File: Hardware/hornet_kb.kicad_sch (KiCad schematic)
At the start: 0 parts

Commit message: Put in mcu and pwoer sheet
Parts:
- added J1: Conn_ST_STDC14, symbol Connector:Conn_ST_STDC14
- added U1: nRF52840, Package_DFN_QFN:Nordic_AQFN-73-1EP_7x7mm_P0.5mm, symbol MCU_Nordic:nRF52840
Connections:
- new net: U1.A22 (VDD), U1.AD14 (VDD), U1.AD23 (VDD), U1.B1 (VDD), U1.W1 (VDD)
- new net: U1.B7 (VSS), U1.EP (VSS)
- new net: J1.5 (GND), J1.7 (GND)
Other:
- added sheet Power Management (power_management.kicad_sch)
- title: (none) -> Hornet Wireless Split Keyboard

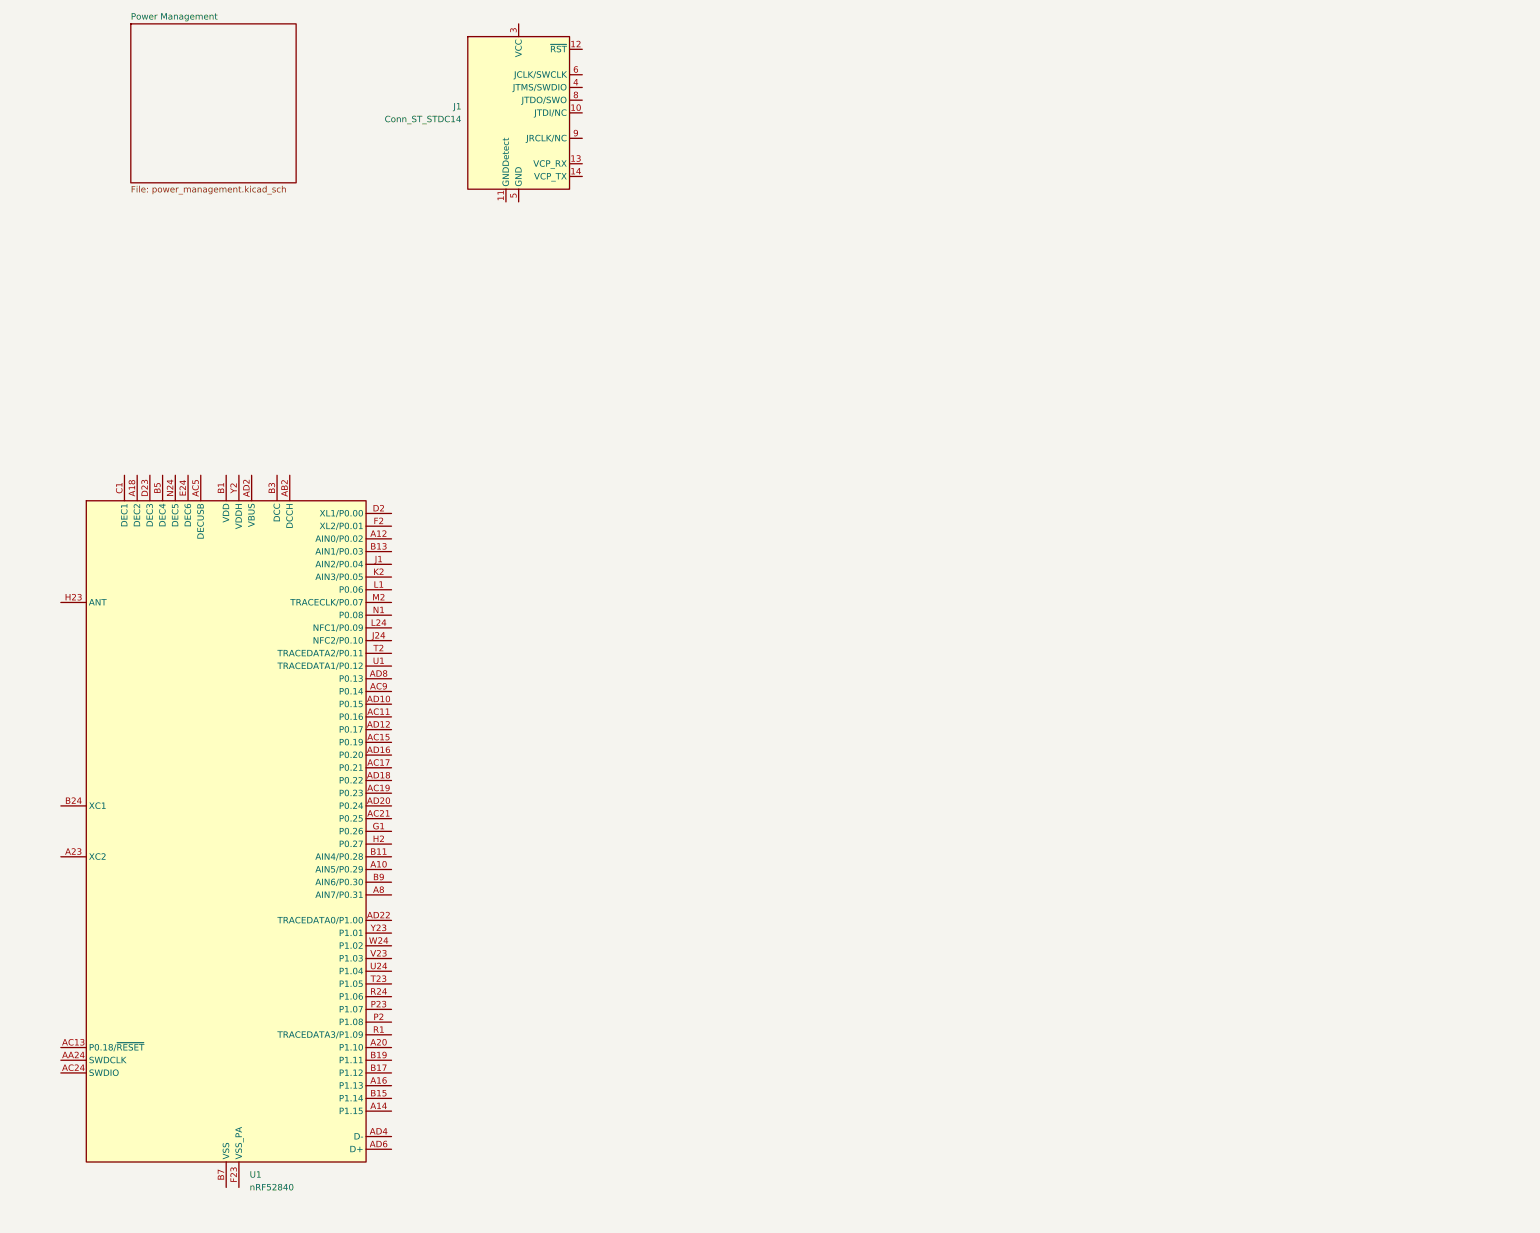
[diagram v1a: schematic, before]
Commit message: Added programmer and usbc
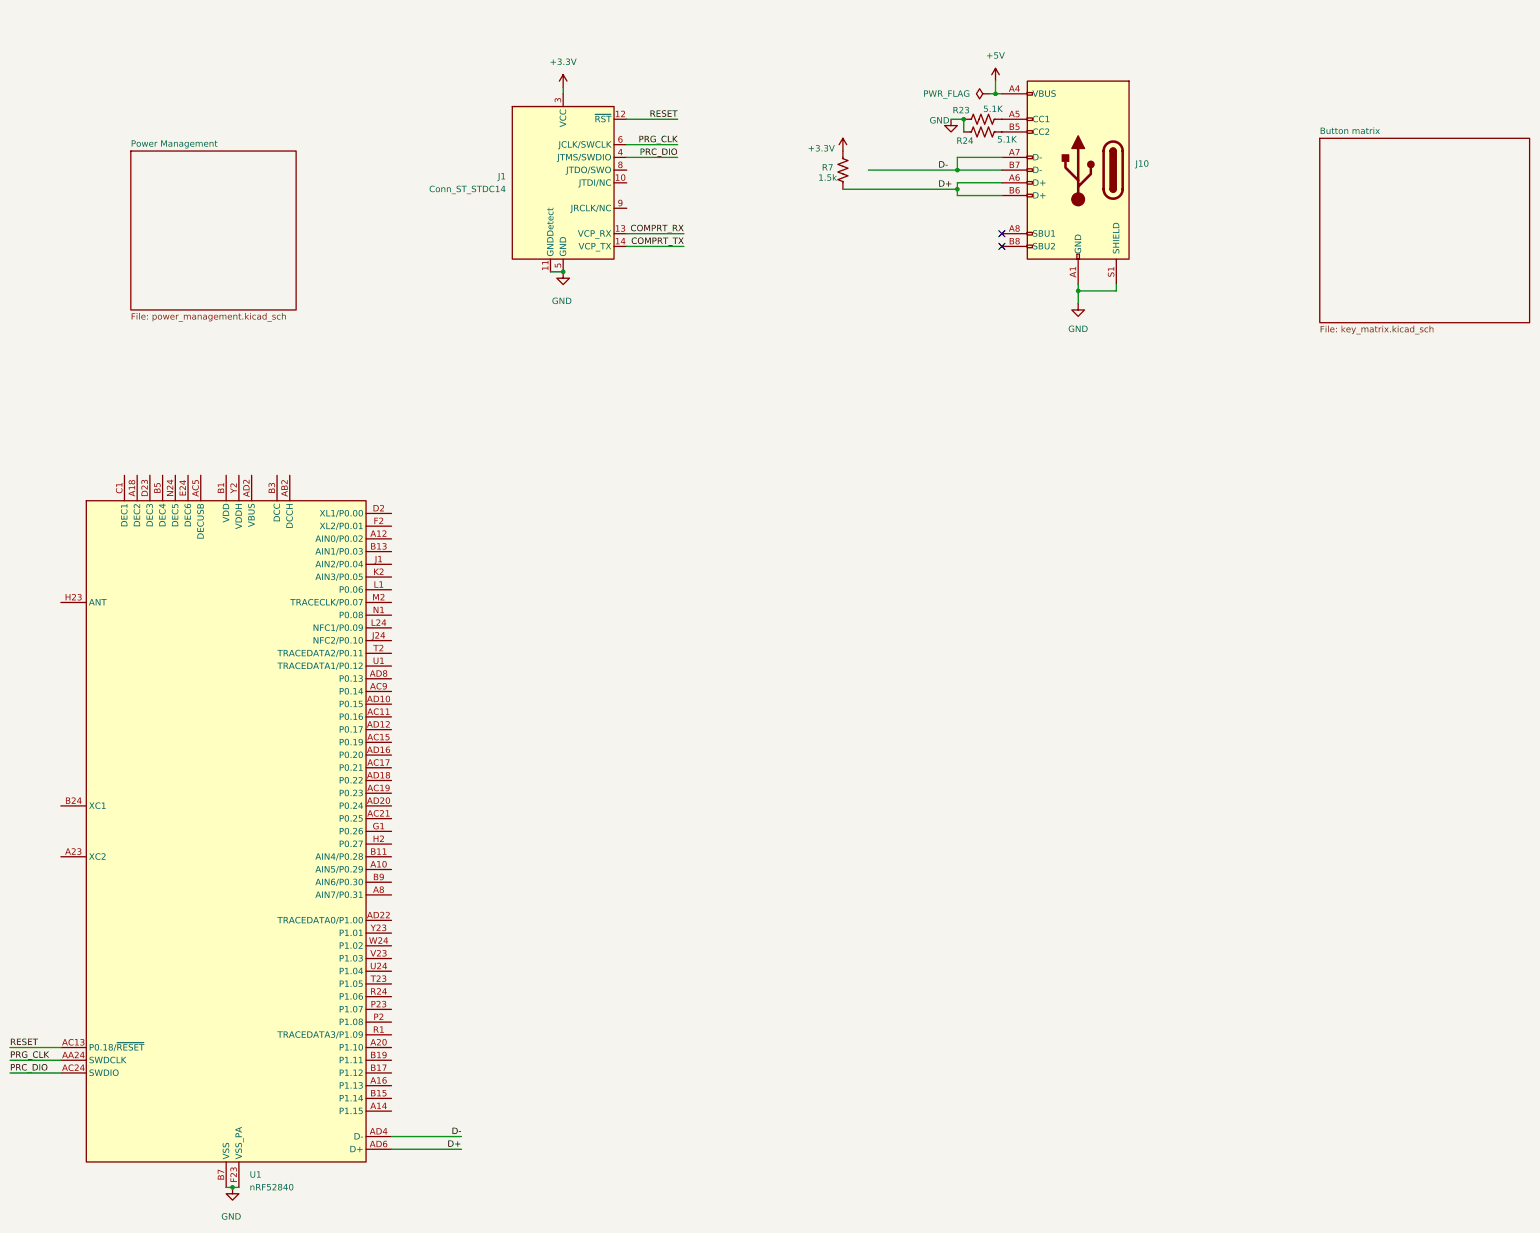
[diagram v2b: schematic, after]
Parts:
- added J10: USB_C_Receptacle_USB2.0, Connector_USB:USB_C_Receptacle_HRO_TYPE-C-31-M-12, symbol Connector:USB_C_Receptacle_USB2.0_16P
- added R23, R24: 5.1K, Resistor_SMD:R_0603_1608Metric, symbol Device:R_US
- added R7: 1.5k, Resistor_SMD:R_0603_1608Metric, symbol Device:R_US
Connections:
- net PRG_CLK: now reaches U1.AA24 (SWDCLK)
- net PRG_CLK: now also J1.6 (JCLK/SWCLK)
- net RESET: now reaches U1.AC13 (P0.18/~{RESET})
- net RESET: now also J1.12 (~{RST})
- net PRC_DIO: now reaches U1.AC24 (SWDIO)
- net PRC_DIO: now also J1.4 (JTMS/SWDIO)
- net D-: now reaches U1.AD4 (D-)
- net D-: now also J10.A7 (D-), J10.B7 (D-)
- net D+: now reaches U1.AD6 (D+)
- net D+: now also J10.A6 (D+), J10.B6 (D+), R7.2
- net GND: now reaches U1.B7 (VSS), U1.EP (VSS)
- net GND: now also J1.11 (GNDDetect), J1.5 (GND), J1.7 (GND), U1.F23 (VSS_PA), J10.A1 (GND), J10.A12 (GND), J10.B1 (GND), J10.B12 (GND), J10.S1 (SHIELD), R23.1, R24.1
- net COMPRT_RX: now reaches J1.13 (VCP_RX)
- net COMPRT_TX: now reaches J1.14 (VCP_TX)
- net +3.3V: now reaches J1.3 (VCC)
- net +3.3V: now also R7.1
- new net: J10.A5 (CC1), R23.2
- new net: J10.B5 (CC2), R24.2
- new net +5V: J10.A4 (VBUS), J10.A9 (VBUS), J10.B4 (VBUS), J10.B9 (VBUS)
- no-connect marks 0 -> 2
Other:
- added sheet Button matrix (key_matrix.kicad_sch)
- moved on the sheet: J1

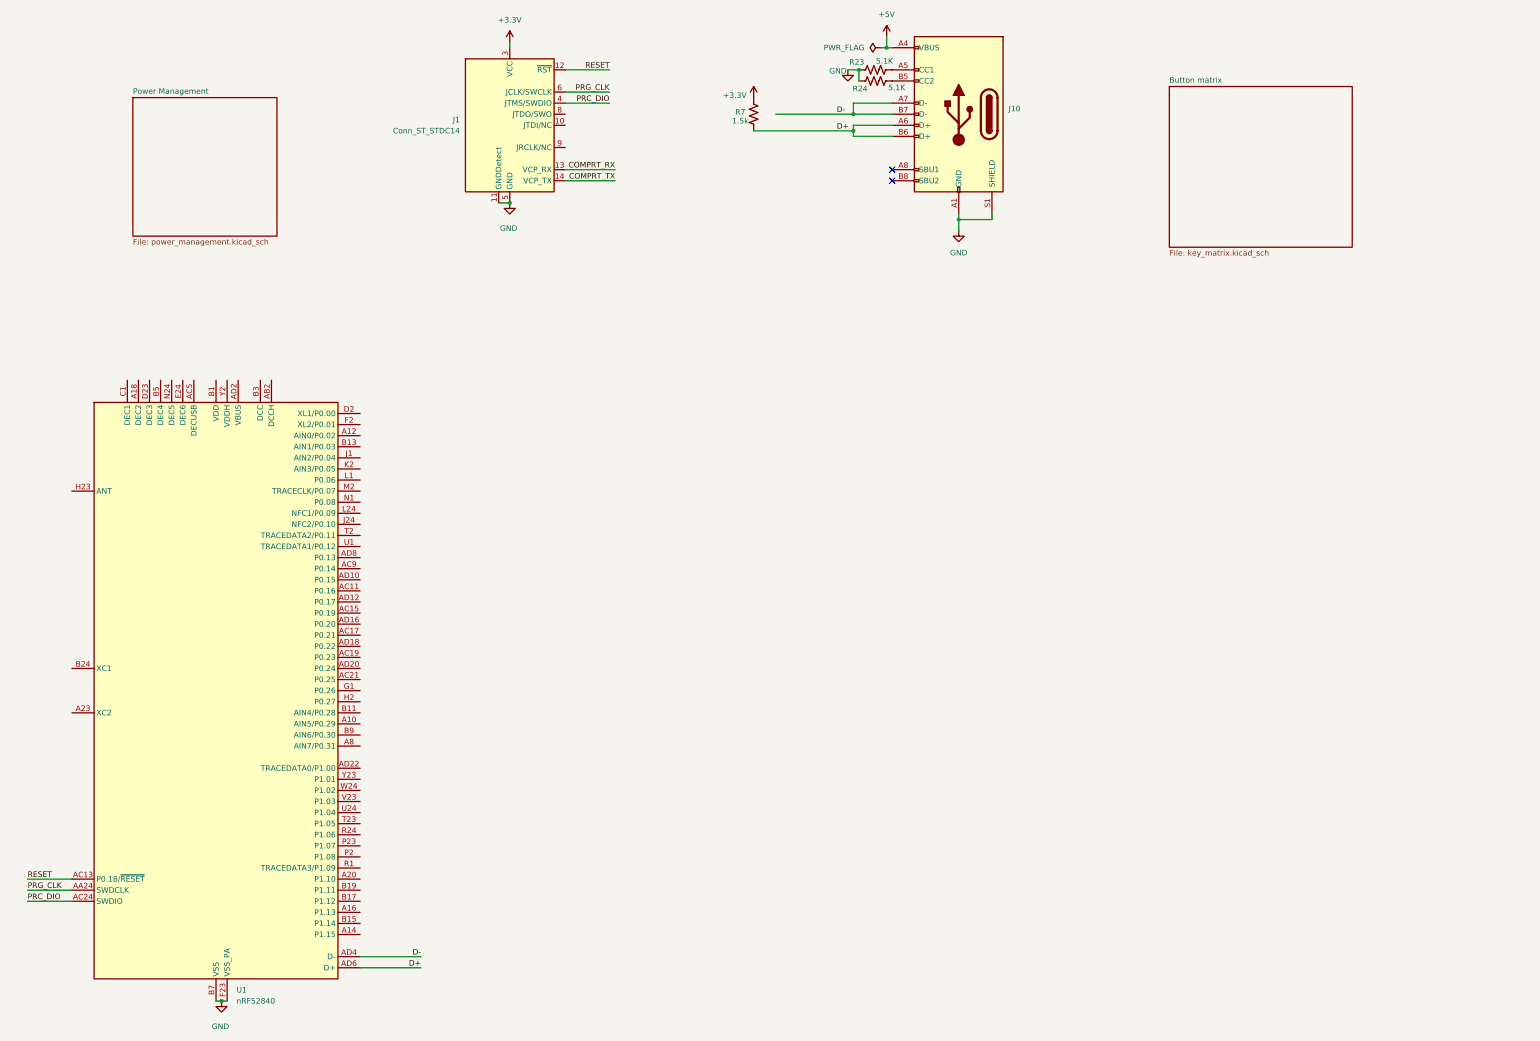
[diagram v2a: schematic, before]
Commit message: added in HS and LSref crystals
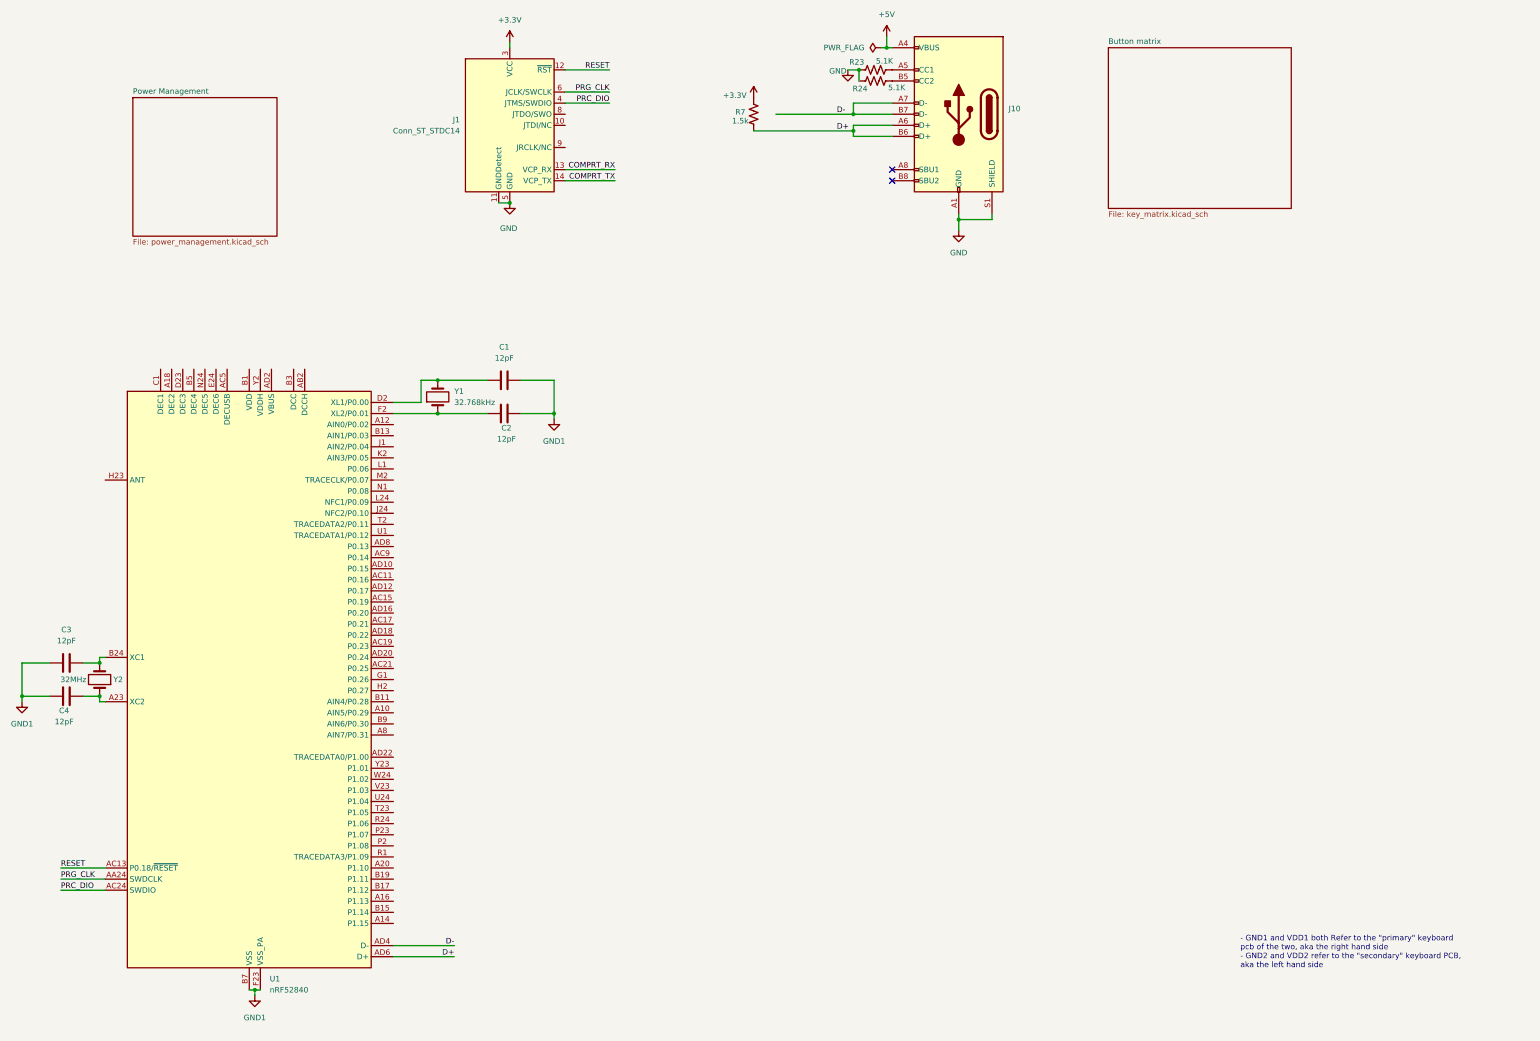
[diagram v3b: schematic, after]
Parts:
- added C1, C2, C3, C4: 12pF, symbol Device:C
- added Y1: 32.768kHz, symbol Device:Crystal
- added Y2: 32MHz, symbol Device:Crystal
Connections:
- net GND: no longer U1.B7 (VSS), U1.EP (VSS), U1.F23 (VSS_PA)
- net at U1.A23 (XC2): now also C4.2, Y2.1
- net at U1.B24 (XC1): now also C3.2, Y2.2
- net at U1.D2 (XL1/P0.00): now also C1.2, Y1.2
- net at U1.F2 (XL2/P0.01): now also C2.2, Y1.1
- new net GND1: C1.1, C2.1, C3.1, C4.1, U1.B7 (VSS), U1.EP (VSS), U1.F23 (VSS_PA)
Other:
- note added: "- GND1 and VDD1 both Refer to the "primary" keyboard pcb of the two, aka the right hand side - GND2 and VDD2 refer to the "secondary" keyboard PCB, aka the left hand side"
- moved on the sheet: U1
